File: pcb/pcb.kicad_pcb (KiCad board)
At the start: 2 copper layers, 90.8 x 63.6 mm, 12 parts, among them SW1 up, SW2 down, SW3 generate, SW4 power sw, U1 MOUDLE-SEEEDUINO-XIAO

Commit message: bcp things
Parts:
- removed powerboost1: ~, power boost 500:powerboost500
- added adafruitbq1: ~, adafruit bq25185:adafruit bq25185, F.Cu at (60.9, 96.9)
- SW1, SW2, SW3: footprint Button_Switch_THT:SW_Tactile_Straight_KSA0Axx1LFTR -> Button_Switch_THT:SW_PUSH_6mm_H5mm
- moved SW4 16.7 mm to (96.5, 109.2)
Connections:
- SSD1306 pad 1: Net-(SSD1306-VCC) -> GND
- SSD1306 pad 2: GND -> Net-(SSD1306-VCC)
- SW4 pad 1: GND -> Net-(adafruitbq1-EN)
- SW4 pad 2: Net-(powerboost1-EN) -> GND
- U1 pad 4: Net-(U1-PA11_A3_D3) -> unconnected-(U1-PA11_A3_D3-Pad4)
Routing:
- net Net-(powerboost1-EN): track 42.5 -> 0.00 mm
- net Net-(U1-PA11_A3_D3): track 40.7 -> 0.00 mm, vias 1 -> 0
- net Net-(adafruitbq1-EN): track 0.00 -> 14.9 mm
- net Net-(U1-5V): track 52.7 -> 39.4 mm
- net Net-(SSD1306-SDA): track 50.8 -> 53.6 mm, vias 0 -> 1
- net Net-(SSD1306-VCC): track 64.4 -> 62.3 mm, vias 0 -> 1
- net Net-(U1-PA10_A2_D2): track 41.2 -> 39.8 mm
- net Net-(SSD1306-SCL): track 46.4 -> 45.5 mm, vias 0 -> 1
- net Net-(U1-PA4_A1_D1): track 75.1 -> 74.6 mm
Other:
- board text added: "SEEEDUINO-XIAO"

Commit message: update pcb
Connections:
- SSD1306 pad 1: GND -> Net-(SSD1306-VCC)
- SSD1306 pad 2: Net-(SSD1306-VCC) -> GND
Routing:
- net Net-(SSD1306-SDA): track 53.6 -> 49.2 mm
- net Net-(SSD1306-VCC): track 62.3 -> 59.8 mm
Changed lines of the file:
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@@
 			)
 		)
-		(pad "1" thru_hole roundrect
+		(pad "1" thru_hole circle
 			(at -3.75 0)
 			(size 2 2)
@@
 			(layers "*.Cu" "*.Mask")
 			(remove_unused_layers no)
-			(roundrect_rratio 0.125)
-			(net "GND")
-			(pinfunction "GND_1")
+			(net "Net-(SSD1306-VCC)")
+			(pinfunction "VCC_1")
 			(pintype "passive")
 		)
-		(pad "2" thru_hole circle
+		(pad "2" thru_hole roundrect
 			(at -1.25 0)
 			(size 2 2)
@@
 			(layers "*.Cu" "*.Mask")
 			(remove_unused_layers no)
-			(net "Net-(SSD1306-VCC)")
-			(pinfunction "VCC_2")
+			(roundrect_rratio 0.125)
+			(net "GND")
+			(pinfunction "GND_2")
 			(pintype "passive")
 		)
@@
 	)
 	(segment
-		(start 68.435 132.82)
-		(end 73.08 132.82)
+		(start 73 129.7)
+		(end 69.88 132.82)
 		(width 0.2)
 		(layer "F.Cu")
@@
 	)
 	(segment
-		(start 73.08 132.82)
-		(end 74.43 131.47)
+		(start 69.88 132.82)
+		(end 68.435 132.82)
 		(width 0.2)
 		(layer "F.Cu")
@@
 	)
 	(via
-		(at 74.43 131.47)
+		(at 73 129.7)
 		(size 0.6)
 		(drill 0.3)
@@
 	)
 	(segment
-		(start 86.457 119.443)
-		(end 103.207 119.443)
+		(start 116.25 103.9)
+		(end 99.95 120.2)
 		(width 0.2)
 		(layer "B.Cu")
@@
 	)
 	(segment
-		(start 103.207 119.443)
-		(end 118.75 103.9)
+		(start 99.95 120.2)
+		(end 82.5 120.2)
 		(width 0.2)
 		(layer "B.Cu")
@@
 	)
 	(segment
-		(start 74.43 131.47)
-		(end 86.457 119.443)
+		(start 82.5 120.2)
+		(end 73 129.7)
 		(width 0.2)
 		(layer "B.Cu")
@@
 	(segment
 		(start 93.97 125.2)
+		(end 93.967 125.203)
+		(width 0.2)
+		(layer "F.Cu")
+		(net "Net-(SSD1306-SCL)")
+	)
+	(segment
+		(start 93.97 125.2)
 		(end 84.6 125.2)
 		(width 0.2)
@@
 	)
 	(segment
-		(start 84.6 127.74)
-		(end 88.65 127.74)
+		(start 93.962372 127.74)
+		(end 93.966596 127.735776)
 		(width 0.2)
 		(layer "F.Cu")
@@
 	)
 	(segment
-		(start 88.65 127.74)
-		(end 90.2 129.29)
+		(start 93.966596 127.735776)
+		(end 93.98082 127.75)
+		(width 0.2)
+		(layer "F.Cu")
+		(net "Net-(SSD1306-SDA)")
+	)
+	(segment
+		(start 84.6 127.74)
+		(end 93.962372 127.74)
 		(width 0.2)
 		(layer "F.Cu")
@@
 	)
 	(via
-		(at 90.2 129.29)
+		(at 93.966596 127.735776)
 		(size 0.6)
 		(drill 0.3)
@@
 	)
 	(segment
-		(start 106.47 121.18)
-		(end 123.75 103.9)
+		(start 93.97082 127.74)
+		(end 93.966596 127.735776)
 		(width 0.2)
 		(layer "B.Cu")
@@
 	)
 	(segment
-		(start 90.2 129.29)
-		(end 103.72 129.29)
+		(start 99.91 127.74)
+		(end 93.97082 127.74)
 		(width 0.2)
 		(layer "B.Cu")
@@
 	)
 	(segment
-		(start 106.47 126.54)
-		(end 106.47 121.18)
-		(width 0.2)
-		(layer "B.Cu")
-		(net "Net-(SSD1306-SDA)")
-	)
-	(segment
-		(start 103.72 129.29)
-		(end 106.47 126.54)
+		(start 99.91 127.74)
+		(end 123.75 103.9)
 		(width 0.2)
 		(layer "B.Cu")

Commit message: update pcb
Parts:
- U1: footprint seed studio xiao:MOUDLE14P-SMD-2.54-21X17.8MM -> seed studio xiao:MOUDLE14P-2.54-21X17.8MM
- moved U1 13.6 mm to (76.8, 130.3), turned to -90 degrees
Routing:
- net Net-(U1-PA02_A0_D0): track 99.4 -> 103.9 mm
- net Net-(U1-PA4_A1_D1): track 74.6 -> 72.7 mm
- net Net-(U1-5V): track 39.4 -> 37.9 mm
- net Net-(SSD1306-VCC): track 59.8 -> 60.5 mm, vias 1 -> 0
- net Net-(SSD1306-SCL): track 45.5 -> 45.7 mm, vias 1 -> 0
- net Net-(SSD1306-SDA): vias 1 -> 0
- removed copper zone on B.Cu, net GND

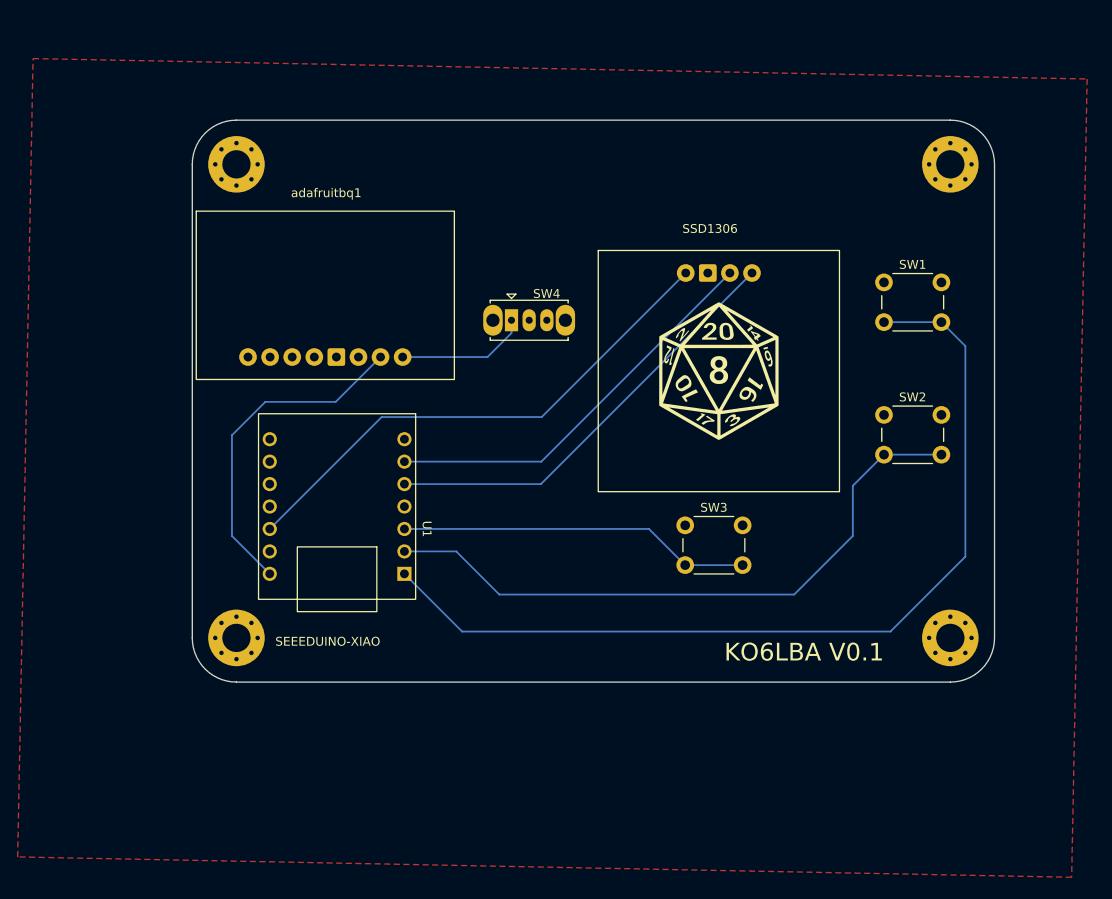
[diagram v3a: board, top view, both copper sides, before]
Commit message: smaller pcb
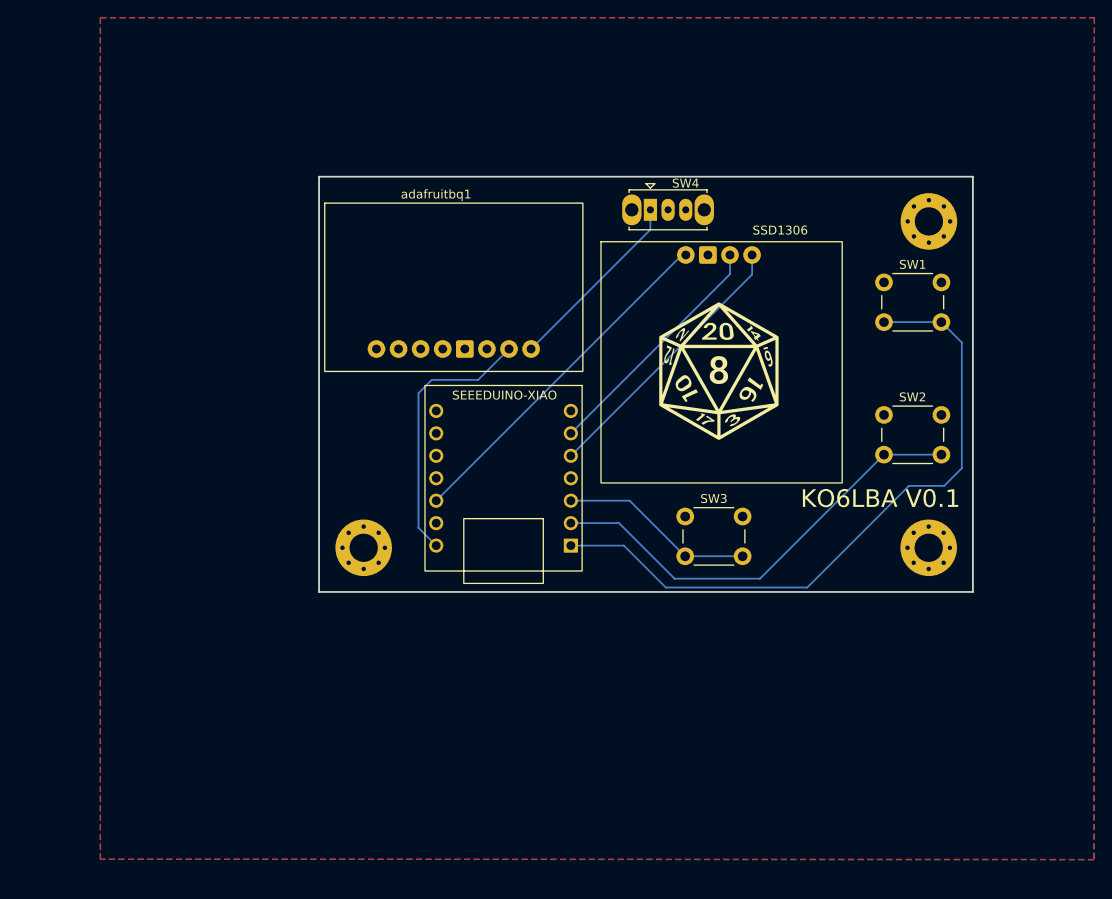
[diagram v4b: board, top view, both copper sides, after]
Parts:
- removed H3: MountingHole_Pad, MountingHole:MountingHole_3.2mm_M3_Pad_Via
- moved H4 91.5 mm to (143.8, 98.1)
- moved H1 45.7 mm to (79.8, 135.0)
- moved SW4 20.1 mm to (112.2, 96.8)
- moved U1 19.1 mm to (95.6, 127.1)
- moved adafruitbq1 14.6 mm to (75.4, 96.0)
- moved SSD1306 13.8 mm to (106.7, 100.4)
- moved H2 10.5 mm to (143.8, 135.0)
- moved SW3 1.00 mm to (116.2, 131.5)
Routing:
- net Net-(U1-PA02_A0_D0): track 103.9 -> 75.8 mm
- net Net-(U1-PA4_A1_D1): track 72.7 -> 50.4 mm
- net Net-(SSD1306-VCC): track 60.5 -> 39.8 mm
- net Net-(SSD1306-SCL): track 45.7 -> 27.6 mm
- net Net-(SSD1306-SDA): track 49.2 -> 31.2 mm
- net Net-(U1-PA10_A2_D2): track 40.0 -> 22.0 mm
- net Net-(U1-5V): track 37.9 -> 30.4 mm
- net Net-(adafruitbq1-EN): track 14.9 -> 21.3 mm
- added copper zone on B.Cu, net (none)
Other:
- board size 90.8 x 63.6 mm -> 74 x 47 mm

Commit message: update board
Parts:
- SW1: value up -> generate
- SW3: value generate -> up
- moved SW1 34.2 mm to (116.8, 131.2)
- moved SW3 32.8 mm to (137.8, 106.7)
- moved SW2 1.05 mm to (137.8, 119.5)
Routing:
- net Net-(U1-PA02_A0_D0): track 75.8 -> 20.4 mm
- net Net-(U1-PA10_A2_D2): track 22.0 -> 48.6 mm
- net Net-(U1-PA4_A1_D1): track 50.4 -> 44.4 mm
- added copper zone on B.Cu, net GND
- removed copper zone on B.Cu, net (none)
